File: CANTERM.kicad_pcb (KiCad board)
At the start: 2 copper layers, 25.4 x 50.8 mm, 9 parts, among them J1 Conn_01x03_Pin, J2 Conn_01x03_Pin, M1 MountingHole_10, M2 MountingHole_10, SW1 SW_DIP_x01

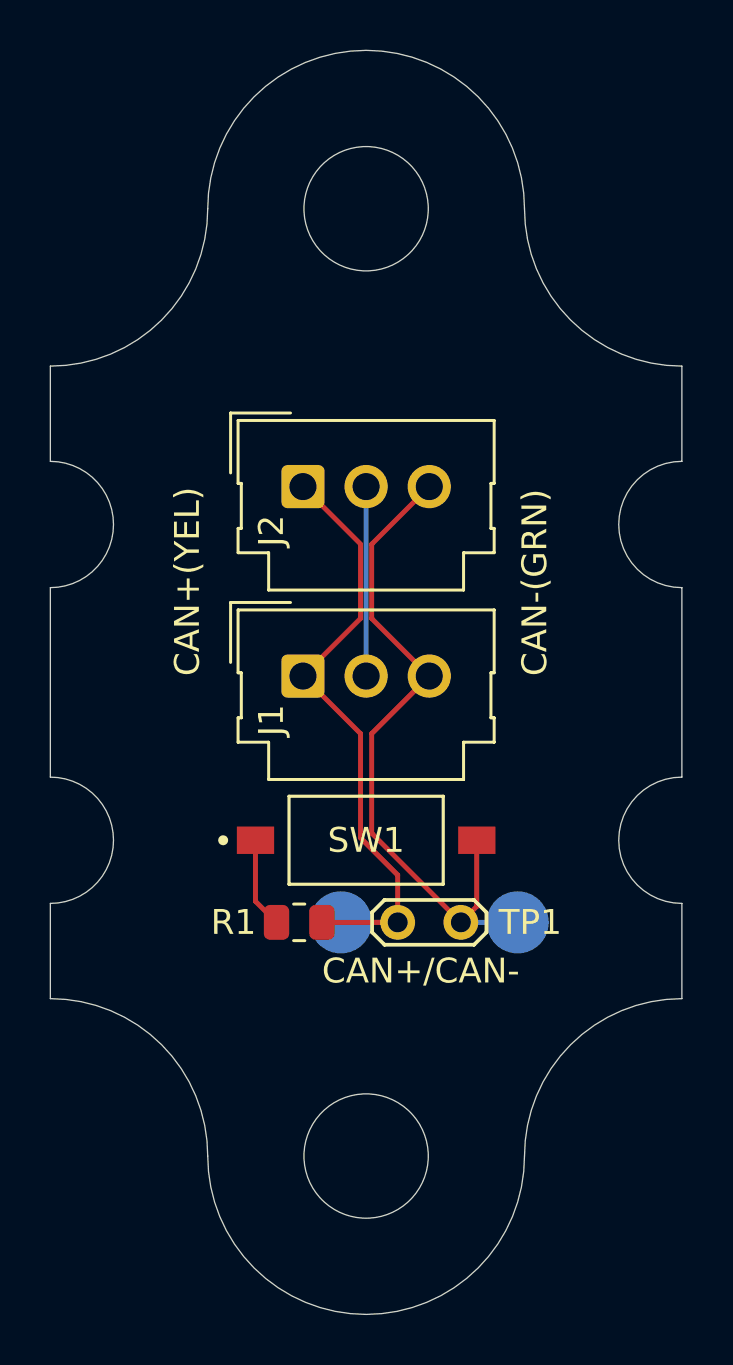
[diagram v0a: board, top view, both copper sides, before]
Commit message: 3rd connector footprint for stub
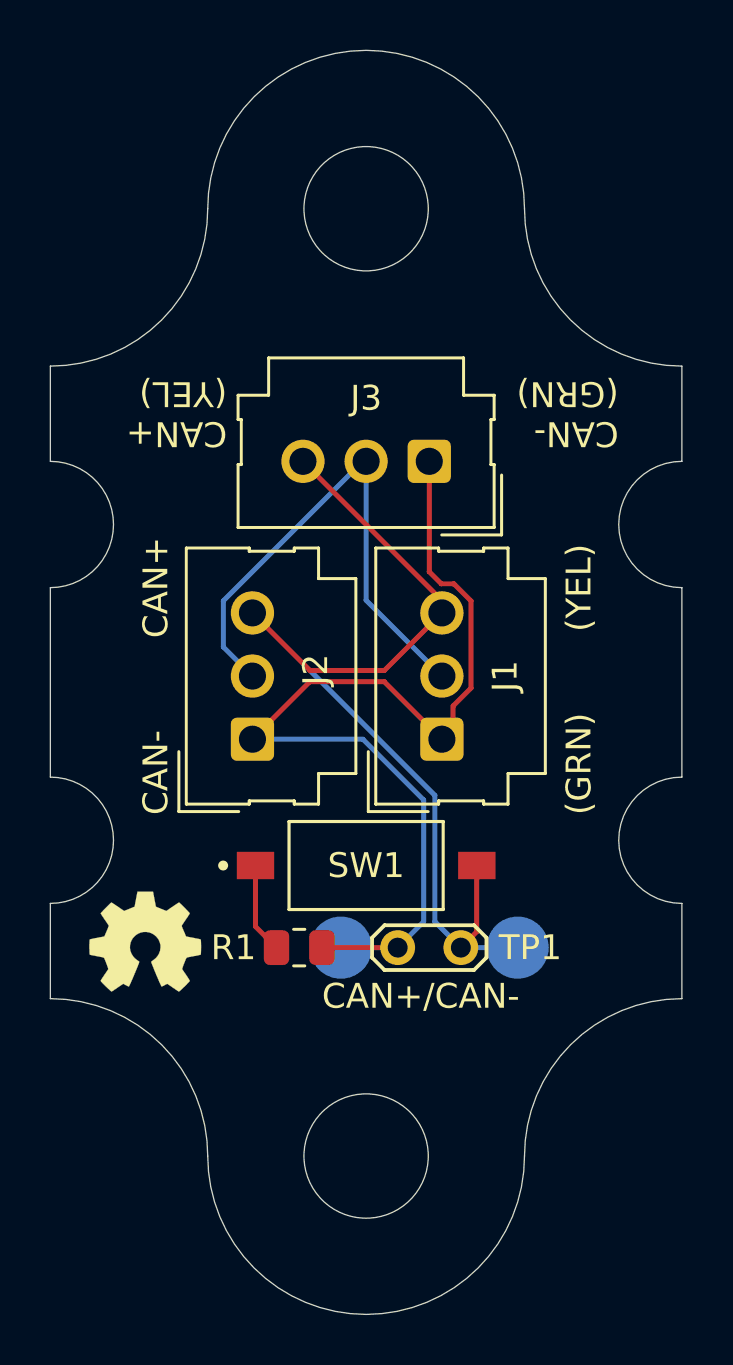
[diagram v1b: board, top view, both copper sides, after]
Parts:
- added J3: Conn_01x03_Pin, Connector_Molex:Molex_SL_171971-0003_1x03_P2.54mm_Vertical, F.Cu at (115.2, 60.2)
- added REF**: OSHW-Logo_XS_SilkScreen, Library:OSHW-Logo_XS_SilkScreen, F.Cu at (103.8, 79.7)
- moved J2 10.4 mm to (108.1, 71.3), turned to 90 degrees
- moved J1 6.14 mm to (115.7, 71.3), turned to 90 degrees
- moved R1 1.02 mm to (110.0, 79.7)
- moved TP1 1.02 mm to (114.0, 79.7)
- moved TP2 1.02 mm to (118.8, 79.7)
- moved TP3 1.02 mm to (111.7, 79.7)
- moved SW1 1.02 mm to (112.7, 76.4)
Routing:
- net CAN-: track 26.4 -> 41.8 mm
- net CENTER: track 7.62 -> 21.5 mm
- net CAN+: track 27.7 -> 40.7 mm
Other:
- rule pad_to_mask_clearance: 0 -> 0.038
- board text added: "(GRN)"
- board text added: "(YEL)"
- board text added: "CAN+"
- board text added: "CAN+ (YEL)"
- board text added: "CAN-"
- board text added: "CAN- (GRN)"
- board text added: "WM CAN Term/Conn Rev 1"
- board text removed: "CAN+(YEL)"
- board text removed: "CAN-(GRN)"

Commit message: remove OSHW logo since I'm not compliant yet
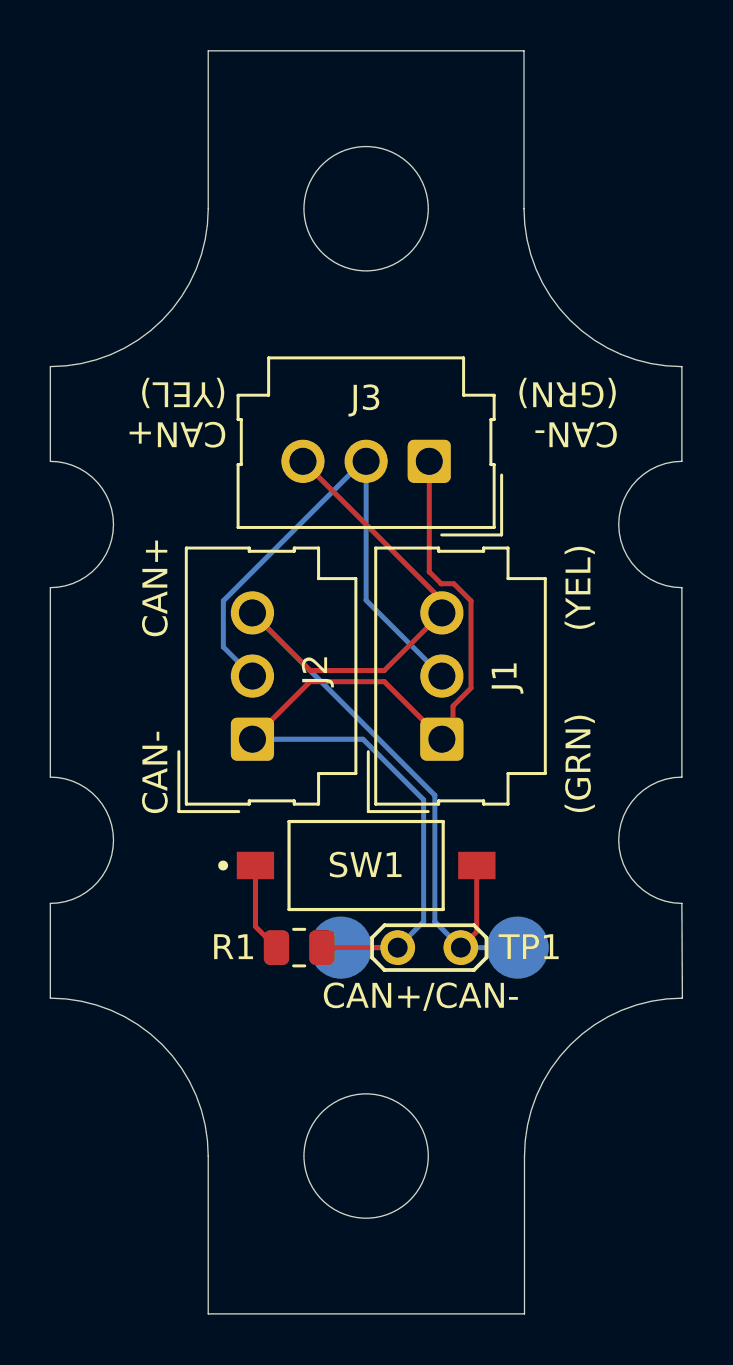
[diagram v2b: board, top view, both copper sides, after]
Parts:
- removed REF**: OSHW-Logo_XS_SilkScreen, Library:OSHW-Logo_XS_SilkScreen
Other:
- outline, holes or cut-outs redrawn

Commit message: wider tracks
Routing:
- net CENTER: track 21.5 -> 24.1 mm
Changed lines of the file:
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@@
 			(layer "F.SilkS"
 				(type "Top Silk Screen")
+				(material "Liquid Photo")
 			)
 			(layer "F.Paste"
@@
 			(layer "B.SilkS"
 				(type "Bottom Silk Screen")
+				(material "Liquid Photo")
 			)
 			(copper_finish "HAL lead-free")
@@
 		)
 		(fp_text user "${REFERENCE}"
-			(at 0 2.54 360)
+			(at 0 2.54 0)
 			(layer "F.Fab")
 			(effects
@@
 		)
 		(property "Value" "Conn_01x03_Pin"
-			(at 2.54 5.25 360)
+			(at 2.54 5.25 0)
 			(layer "F.Fab")
 			(effects
@@
 		)
 		(fp_text user "${REFERENCE}"
-			(at 2.54 1.85 360)
+			(at 2.54 1.85 0)
 			(layer "F.Fab")
 			(effects
@@
 		)
 	)
-	(gr_text "CAN-/CAN+"
+	(gr_text "CAN+/CAN-"
 		(at 119.558 82.766 0)
 		(layer "B.SilkS")
@@
 		)
 	)
-	(gr_text "CAN+/CAN-"
+	(gr_text "CAN-/CAN+"
 		(at 110.922 82.258 0)
 		(layer "F.SilkS")
@@
 	)
 	(segment
-		(start 117.15 79.078)
-		(end 116.51 79.718)
-		(width 0.2)
+		(start 110.16 60.16)
+		(end 115.748 65.748)
+		(width 0.254)
 		(layer "F.Cu")
 		(net 1)
 	)
 	(segment
-		(start 117.15 76.416)
-		(end 117.15 79.078)
-		(width 0.2)
+		(start 115.748 65.748)
+		(end 115.748 66.256)
+		(width 0.254)
 		(layer "F.Cu")
 		(net 1)
 	)
 	(segment
-		(start 108.128 66.256)
-		(end 110.442999 68.570999)
-		(width 0.2)
+		(start 110.416 68.544)
+		(end 108.128 66.256)
+		(width 0.254)
 		(layer "F.Cu")
 		(net 1)
 	)
 	(segment
-		(start 115.748 65.748)
-		(end 110.16 60.16)
-		(width 0.2)
+		(start 116.51 77.056)
+		(end 117.15 76.416)
+		(width 0.254)
 		(layer "F.Cu")
 		(net 1)
 	)
 	(segment
-		(start 113.433001 68.570999)
-		(end 115.748 66.256)
-		(width 0.2)
+		(start 115.748 66.256)
+		(end 113.46 68.544)
+		(width 0.254)
 		(layer "F.Cu")
 		(net 1)
 	)
 	(segment
-		(start 110.442999 68.570999)
-		(end 113.433001 68.570999)
-		(width 0.2)
+		(start 116.51 79.718)
+		(end 116.51 77.056)
+		(width 0.254)
 		(layer "F.Cu")
 		(net 1)
 	)
 	(segment
-		(start 115.748 66.256)
-		(end 115.748 65.748)
-		(width 0.2)
+		(start 113.46 68.544)
+		(end 110.416 68.544)
+		(width 0.254)
 		(layer "F.Cu")
 		(net 1)
 	)
 	(segment
-		(start 116.51 79.718)
+		(start 115.465001 73.593001)
 		(end 115.465001 78.673001)
 		(width 0.2)
@@
 	)
 	(segment
-		(start 115.465001 73.593001)
-		(end 108.128 66.256)
+		(start 115.465001 78.673001)
+		(end 116.51 79.718)
 		(width 0.2)
 		(layer "B.Cu")
@@
 		(start 116.51 79.718)
 		(end 118.796 79.718)
-		(width 0.2)
+		(width 0.254)
 		(layer "B.Cu")
 		(net 1)
 	)
 	(segment
-		(start 115.465001 78.673001)
+		(start 108.128 66.256)
 		(end 115.465001 73.593001)
 		(width 0.2)
@@
 	)
 	(segment
-		(start 110.922 79.718)
-		(end 113.97 79.718)
-		(width 0.2)
+		(start 113.46 69.048)
+		(end 110.416 69.048)
+		(width 0.254)
 		(layer "F.Cu")
 		(net 2)
 	)
 	(segment
-		(start 115.24 64.603603)
-		(end 115.24 60.16)
-		(width 0.2)
+		(start 115.24 60.16)
+		(end 115.24 64.527236)
+		(width 0.254)
 		(layer "F.Cu")
 		(net 2)
 	)
 	(segment
-		(start 113.433001 69.021001)
-		(end 115.748 71.336)
-		(width 0.2)
+		(start 116.252 69.984814)
+		(end 116.252 70.832)
+		(width 0.254)
 		(layer "F.Cu")
 		(net 2)
 	)
 	(segment
-		(start 108.128 71.336)
-		(end 110.442999 69.021001)
-		(width 0.2)
+		(start 115.748 71.336)
+		(end 113.46 69.048)
+		(width 0.254)
 		(layer "F.Cu")
 		(net 2)
 	)
 	(segment
-		(start 116.918 69.28063)
-		(end 116.918 65.77137)
-		(width 0.2)
+		(start 116.252 70.832)
+		(end 115.748 71.336)
+		(width 0.254)
 		(layer "F.Cu")
 		(net 2)
 	)
 	(segment
-		(start 116.918 65.77137)
-		(end 116.23263 65.086)
-		(width 0.2)
+		(start 116.945 65.760186)
+		(end 116.945 69.291814)
+		(width 0.254)
 		(layer "F.Cu")
 		(net 2)
 	)
 	(segment
-		(start 116.23263 65.086)
-		(end 115.722397 65.086)
-		(width 0.2)
+		(start 115.24 64.527236)
+		(end 115.771764 65.059)
+		(width 0.254)
 		(layer "F.Cu")
 		(net 2)
 	)
 	(segment
-		(start 110.442999 69.021001)
-		(end 113.433001 69.021001)
-		(width 0.2)
+		(start 115.771764 65.059)
+		(end 116.243814 65.059)
+		(width 0.254)
 		(layer "F.Cu")
 		(net 2)
 	)
 	(segment
-		(start 115.722397 65.086)
-		(end 115.24 64.603603)
-		(width 0.2)
+		(start 110.416 69.048)
+		(end 108.128 71.336)
+		(width 0.254)
 		(layer "F.Cu")
 		(net 2)
 	)
 	(segment
-		(start 115.748 71.336)
-		(end 116.198 70.886)
-		(width 0.2)
+		(start 113.97 79.718)
+		(end 110.922 79.718)
+		(width 0.254)
 		(layer "F.Cu")
 		(net 2)
 	)
 	(segment
-		(start 116.198 70.00063)
-		(end 116.918 69.28063)
-		(width 0.2)
+		(start 116.945 69.291814)
+		(end 116.252 69.984814)
+		(width 0.254)
 		(layer "F.Cu")
 		(net 2)
 	)
 	(segment
-		(start 116.198 70.886)
-		(end 116.198 70.00063)
-		(width 0.2)
+		(start 116.243814 65.059)
+		(end 116.945 65.760186)
+		(width 0.254)
 		(layer "F.Cu")
 		(net 2)
 	)
 	(segment
-		(start 113.97 79.718)
-		(end 115.014999 78.673001)
+		(start 108.128 71.336)
+		(end 112.571603 71.336)
 		(width 0.2)
 		(layer "B.Cu")
@@
 	)
 	(segment
-		(start 115.014999 73.779396)
-		(end 112.571603 71.336)
+		(start 115.014999 78.673001)
+		(end 113.97 79.718)
 		(width 0.2)
 		(layer "B.Cu")
@@
 	)
 	(segment
-		(start 113.97 79.718)
-		(end 111.684 79.718)
+		(start 112.571603 71.336)
+		(end 115.014999 73.779396)
 		(width 0.2)
 		(layer "B.Cu")
@@
 	)
 	(segment
-		(start 112.571603 71.336)
-		(end 108.128 71.336)
+		(start 115.014999 73.779396)
+		(end 115.014999 78.673001)
 		(width 0.2)
 		(layer "B.Cu")
@@
 	)
 	(segment
-		(start 115.014999 78.673001)
-		(end 115.014999 73.779396)
-		(width 0.2)
+		(start 113.97 79.718)
+		(end 111.684 79.718)
+		(width 0.254)
 		(layer "B.Cu")
 		(net 2)
 	)
 	(segment
-		(start 106.958 65.77137)
-		(end 106.958 67.626)
-		(width 0.2)
+		(start 112.7 65.748)
+		(end 115.748 68.796)
+		(width 0.254)
 		(layer "B.Cu")
 		(net 3)
 	)
 	(segment
-		(start 112.7 65.748)
-		(end 115.748 68.796)
-		(width 0.2)
+		(start 107.632186 65.059)
+		(end 112.011 65.059)
+		(width 0.254)
 		(layer "B.Cu")
 		(net 3)
 	)
 	(segment
-		(start 112.56937 60.16)
-		(end 106.958 65.77137)
-		(width 0.2)
+		(start 108.128 68.796)
+		(end 108.128 67.948814)
+		(width 0.254)
 		(layer "B.Cu")
 		(net 3)
@@
 		(start 112.7 60.16)
 		(end 112.7 65.748)
-		(width 0.2)
+		(width 0.254)
 		(layer "B.Cu")
 		(net 3)
 	)
 	(segment
-		(start 106.958 67.626)
-		(end 108.128 68.796)
-		(width 0.2)
+		(start 106.931 66.751814)
+		(end 106.931 65.760186)
+		(width 0.254)
 		(layer "B.Cu")
 		(net 3)
 	)
 	(segment
-		(start 112.7 60.16)
-		(end 112.56937 60.16)
-		(width 0.2)
+		(start 112.011 65.059)
+		(end 115.748 68.796)
+		(width 0.254)
 		(layer "B.Cu")
 		(net 3)
 	)
 	(segment
-		(start 108.25 78.871)
-		(end 109.097 79.718)
-		(width 0.2)
+		(start 108.128 67.948814)
+		(end 106.931 66.751814)
+		(width 0.254)
+		(layer "B.Cu")
+		(net 3)
+	)
+	(segment
+		(start 106.931 65.760186)
+		(end 107.632186 65.059)
+		(width 0.254)
+		(layer "B.Cu")
+		(net 3)
+	)
+	(segment
+		(start 109.097 77.263)
+		(end 108.25 76.416)
+		(width 0.254)
 		(layer "F.Cu")
 		(net 4)
 	)
 	(segment
-		(start 108.25 76.416)
-		(end 108.25 78.871)
-		(width 0.2)
+		(start 109.097 79.718)
+		(end 109.097 77.263)
+		(width 0.254)
 		(layer "F.Cu")
 		(net 4)

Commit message: initial release
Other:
- board text added: "WM CAN Term/Conn Rev 2"
- board text removed: "WM CAN Term/Conn Rev 1"
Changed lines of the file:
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@@
 		(layer "User.9")
 	)
-	(gr_text "WM CAN Term/Conn\nRev 1"
+	(gr_text "WM CAN Term/Conn\nRev 2"
 		(at 106.35 56.604 90)
 		(layer "B.SilkS")
@@
 	)
 	(segment
-		(start 115.465001 73.593001)
-		(end 115.465001 78.673001)
-		(width 0.2)
-		(layer "B.Cu")
-		(net 1)
-	)
-	(segment
-		(start 115.465001 78.673001)
-		(end 116.51 79.718)
-		(width 0.2)
+		(start 115.492 73.62)
+		(end 108.128 66.256)
+		(width 0.254)
+		(layer "B.Cu")
+		(net 1)
+	)
+	(segment
+		(start 115.492 78.7)
+		(end 115.492 73.62)
+		(width 0.254)
 		(layer "B.Cu")
 		(net 1)
@@
 	)
 	(segment
-		(start 108.128 66.256)
-		(end 115.465001 73.593001)
-		(width 0.2)
+		(start 116.51 79.718)
+		(end 115.492 78.7)
+		(width 0.254)
 		(layer "B.Cu")
 		(net 1)
@@
 	)
 	(segment
-		(start 108.128 71.336)
-		(end 112.571603 71.336)
-		(width 0.2)
-		(layer "B.Cu")
-		(net 2)
-	)
-	(segment
-		(start 115.014999 78.673001)
-		(end 113.97 79.718)
-		(width 0.2)
-		(layer "B.Cu")
-		(net 2)
-	)
-	(segment
-		(start 112.571603 71.336)
-		(end 115.014999 73.779396)
-		(width 0.2)
-		(layer "B.Cu")
-		(net 2)
-	)
-	(segment
-		(start 115.014999 73.779396)
-		(end 115.014999 78.673001)
-		(width 0.2)
-		(layer "B.Cu")
-		(net 2)
+		(start 114.988 73.828764)
+		(end 112.495236 71.336)
+		(width 0.254)
+		(layer "B.Cu")
+		(net 2)
+	)
+	(segment
+		(start 112.495236 71.336)
+		(end 108.128 71.336)
+		(width 0.254)
+		(layer "B.Cu")
+		(net 2)
+	)
+	(segment
+		(start 113.97 79.718)
+		(end 114.988 78.7)
+		(width 0.254)
+		(layer "B.Cu")
+		(net 2)
+	)
+	(segment
+		(start 114.988 78.7)
+		(end 114.988 73.828764)
+		(width 0.254)
+		(layer "B.Cu")
+		(net 2)
